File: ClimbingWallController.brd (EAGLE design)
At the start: 100 x 80 mm, 336 parts, among them IC1 74HCT138D, IC2 74HCT138D, IC3 PIC24FJ32GB004, IC4 SN74LV4052AD, IC5 SN74LV4052AD, IC6 TC1015, IC7 NCP1117, J1 PWR, Q1 DPBT8105, Q10 DPBT8105, Q11 DPBT8105, Q12 DPBT8105, Q13 DPBT8105, Q14 DPBT8105, Q15 DPBT8105, Q16 DPBT8105, Q17 NC, Q2 DPBT8105, Q3 DPBT8105, Q4 DPBT8105, Q5 DPBT8105, Q6 DPBT8105, Q7 DPBT8105, Q8 DPBT8105, Q9 DPBT8105, X1 MINI-USB-32005-201

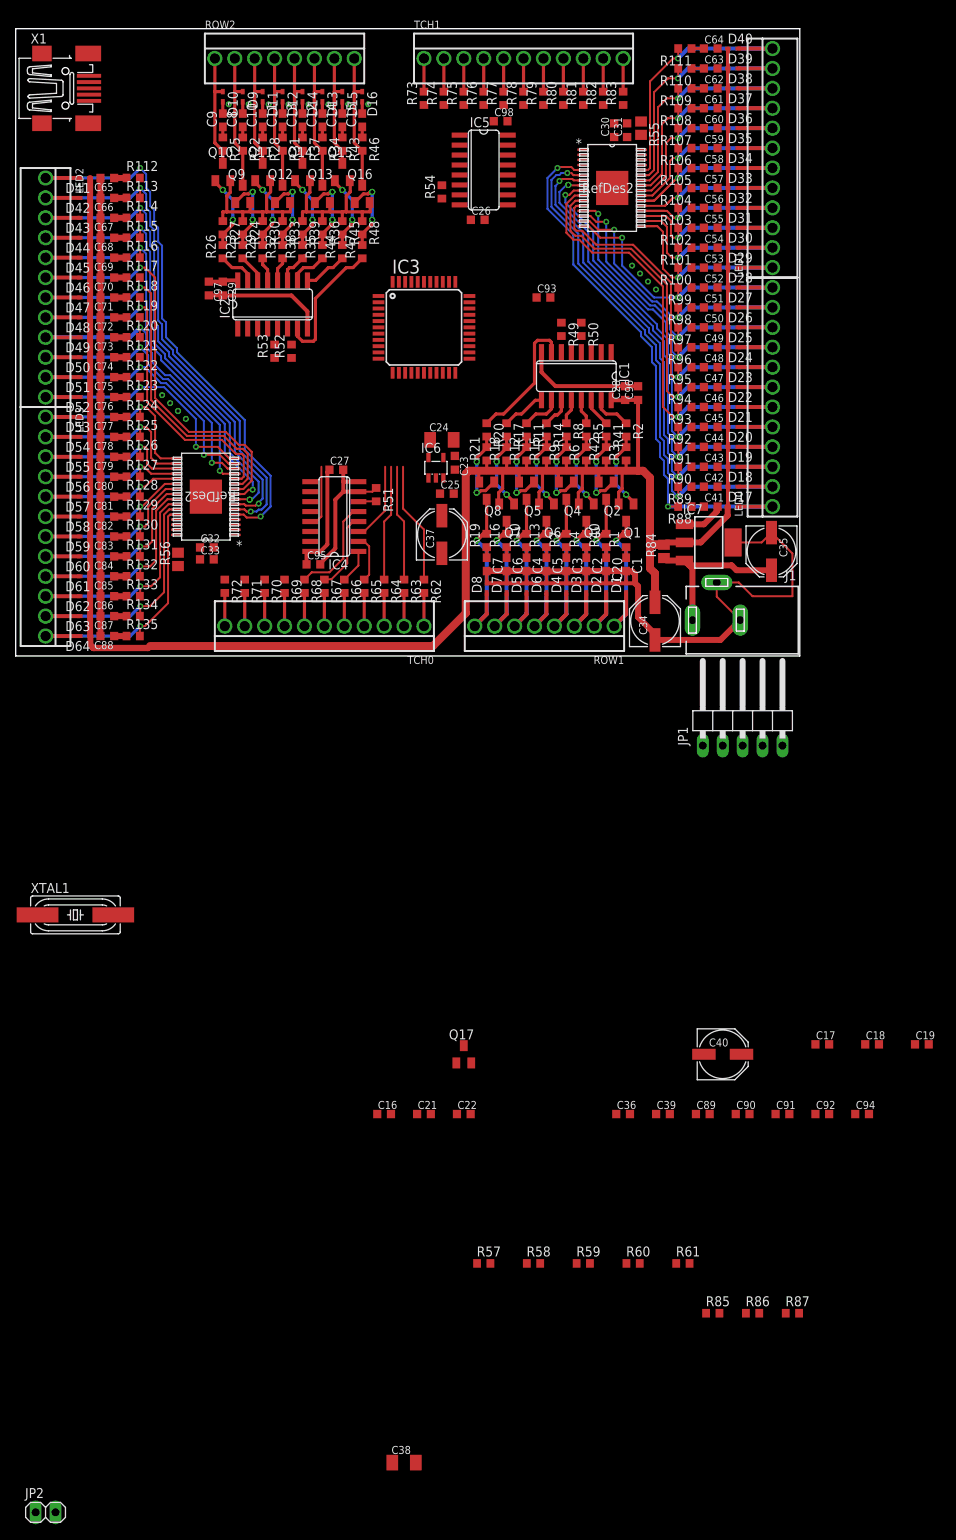
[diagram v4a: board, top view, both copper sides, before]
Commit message: Completed routing of all circuit board elements. Created ground fills, and stitched everything together. Need to review sensitive signal coupling and review decoupling paths. Need to verify footprints.
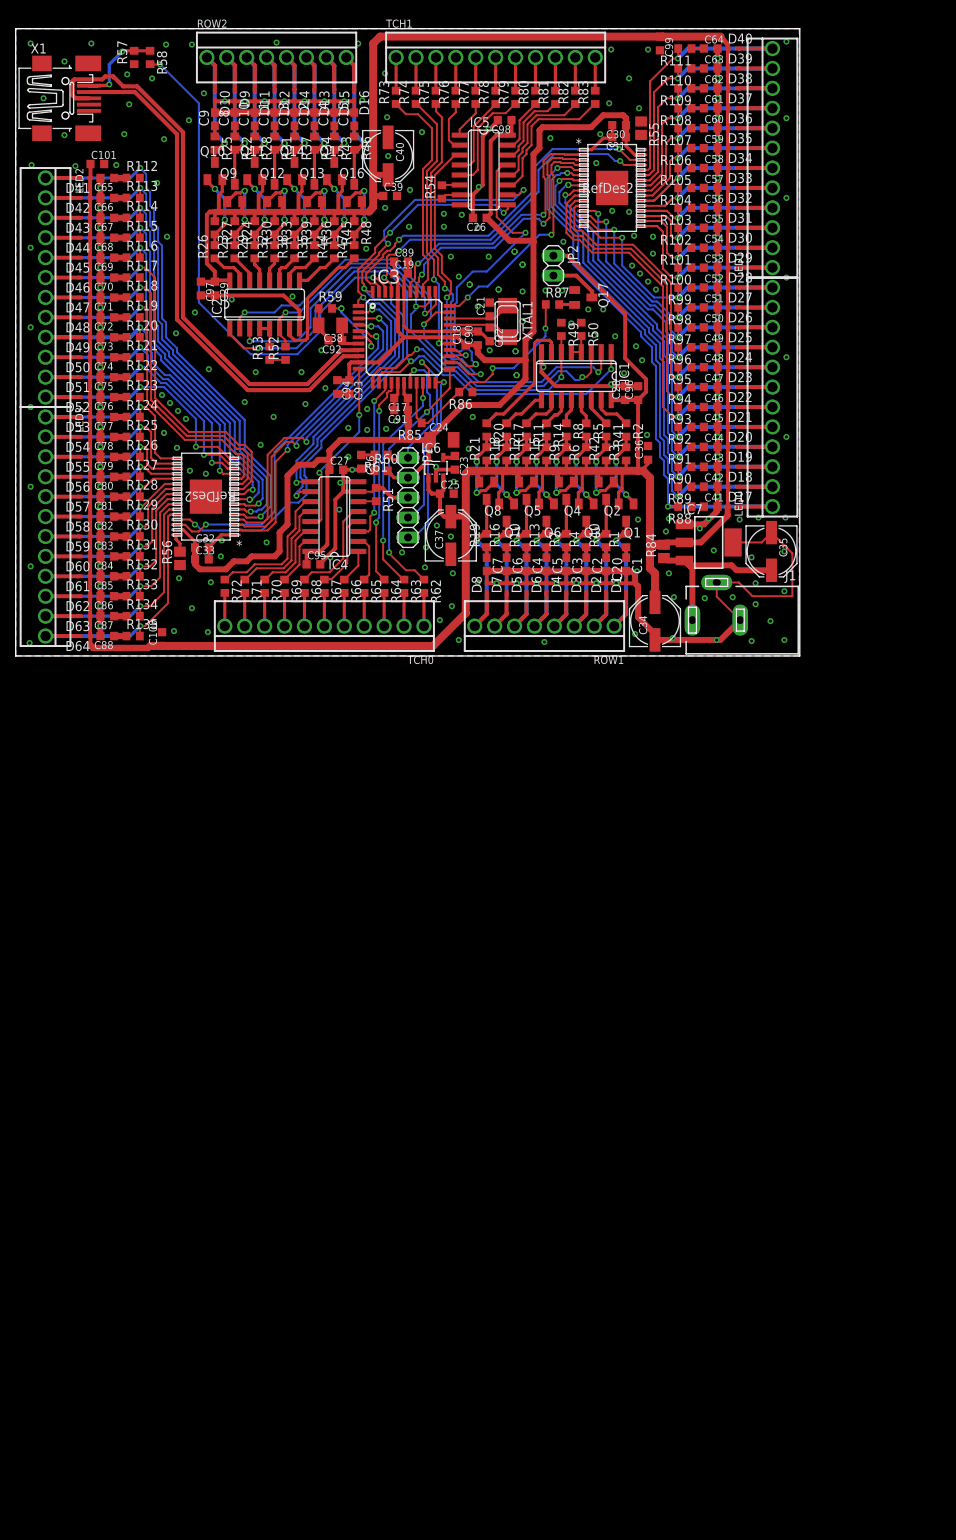
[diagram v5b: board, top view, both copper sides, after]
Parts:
- added C100, C101, C99: 0.1uF, rcl:C0603K
- JP1: device pinhead:1X05/90 -> pinhead:1X05
- XTAL1: device crystal:HC49UP -> Parts:NX5032
- moved JP2 171.7 mm to (68.6, 49.8), turned to 270 degrees
- moved R58 161.4 mm to (17.1, 76.3), turned to 270 degrees
- moved R57 160.1 mm to (15.1, 76.3), turned to 90 degrees
- moved C38 145.3 mm to (40.1, 42.2), turned to 180 degrees
- moved R87 132.2 mm to (68.5, 44.8)
- moved R59 126.2 mm to (39.5, 44.3)
- moved R86 123.0 mm to (57.4, 33.7), turned to 180 degrees
- moved C40 122.2 mm to (47.5, 63.8), turned to 270 degrees
- moved C39 122.2 mm to (47.8, 58.7)
- moved R85 119.7 mm to (50.9, 29.7), turned to 180 degrees
- moved C19 118.6 mm to (49.1, 48.8)
- moved C92 116.6 mm to (40.8, 40.3), turned to 180 degrees
- moved C89 115.3 mm to (49.1, 50.3)
- moved C94 114.3 mm to (41.0, 34.3), turned to 270 degrees
- moved R61 110.1 mm to (46.6, 25.7), turned to 180 degrees
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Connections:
- removed net N$86: R85.1, R86.2
- net +5V: now also C100.1, C101.1, C99.1
- net GND: now also C100.2, C101.2, C99.2
- net OSCI: now also XTAL1.P$1; no longer XTAL1.1
- net OSCO: now also XTAL1.P$2; no longer XTAL1.2
- net TMUX0: now also IC3.14; no longer IC3.11
- net TMUX1: now also IC3.11; no longer IC3.14
- net TOUCH11: now also IC3.36; no longer IC5.1
- net TOUCH12: now also IC3.27; no longer IC5.5
- net TOUCH13: now also IC3.26; no longer IC5.2
- net TOUCH14: now also IC5.2; no longer IC5.4
- net TOUCH15: now also IC5.1; no longer IC5.12
- net TOUCH16: now also IC5.4; no longer IC5.14
- net TOUCH17: now also IC5.5; no longer IC5.15
- net TOUCH18: now also IC5.15; no longer IC5.11
- net TOUCH19: now also IC5.14; no longer IC3.26
- net TOUCH20: now also IC5.12; no longer IC3.27
- net TOUCH21: now also IC5.11; no longer IC3.36
- net VREF+: now also R85.1, R86.2
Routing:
- net +3V3: track 14.5 -> 209.4 mm
- net GND: track 236.1 -> 387.7 mm, vias 0 -> 238
- net +5V: track 338.9 -> 487.4 mm
- net C_BLANK: track 0.00 -> 98.3 mm, vias 0 -> 4
- net RSEL0: track 0.00 -> 76.8 mm, vias 0 -> 3
- net D+: track 0.00 -> 72.7 mm
- net AMSEL0: track 0.00 -> 68.9 mm, vias 0 -> 4
- net RSEL1: track 0.00 -> 68.6 mm, vias 0 -> 3
- net RSEL2: track 0.00 -> 68.5 mm, vias 0 -> 3
- net N$45: track 0.00 -> 66.8 mm, vias 0 -> 2
- net D-: track 0.00 -> 65.8 mm
- net AMSEL1: track 0.00 -> 62.4 mm, vias 0 -> 4
- net C0_SOUT: track 0.00 -> 47.8 mm, vias 0 -> 2
- net C1_SOUT: track 0.00 -> 44.4 mm, vias 0 -> 2
- net C1_LAT: track 0.00 -> 43.4 mm, vias 0 -> 2
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- added copper zone on layer 1, net GND
- added copper zone on layer 16, net GND

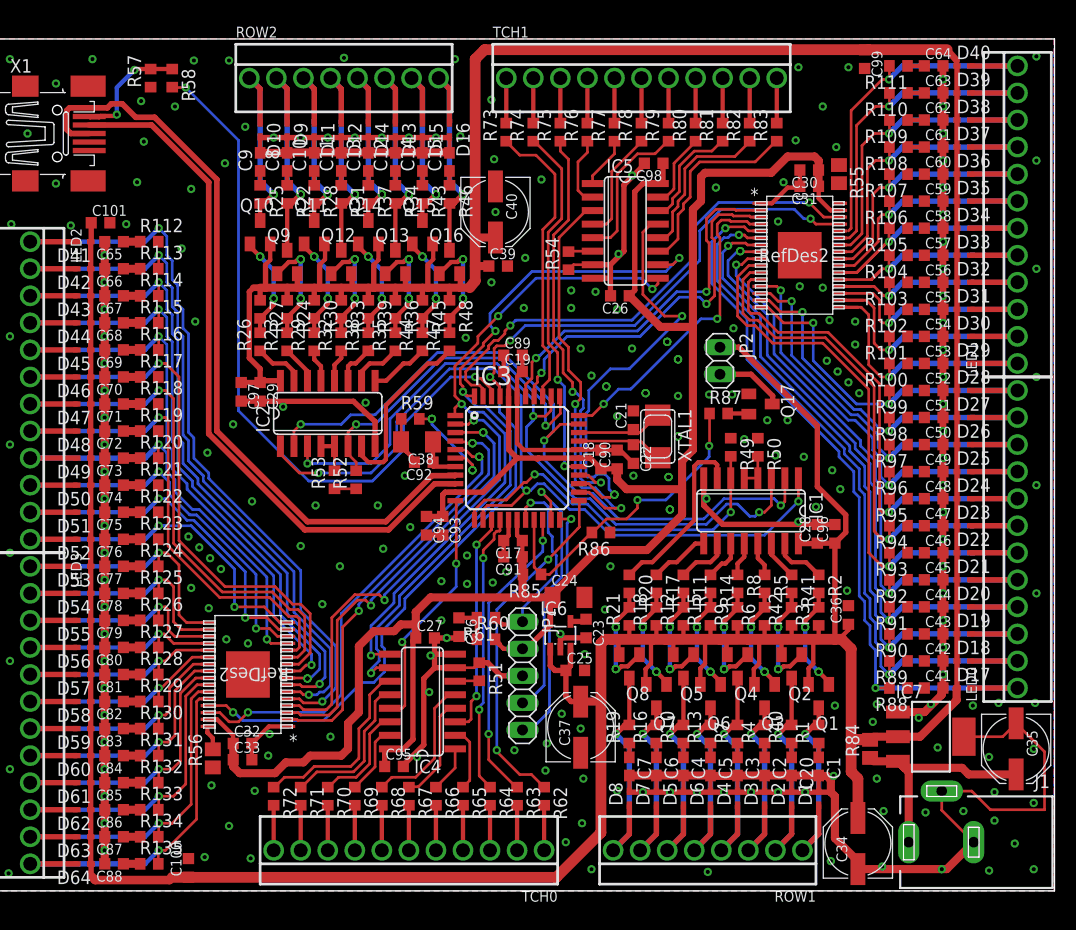
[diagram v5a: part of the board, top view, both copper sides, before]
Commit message: Cleaned up floating ratsnest wires. Cleaned up DRC Errors. Need to check DRC with SEEED's rule set.
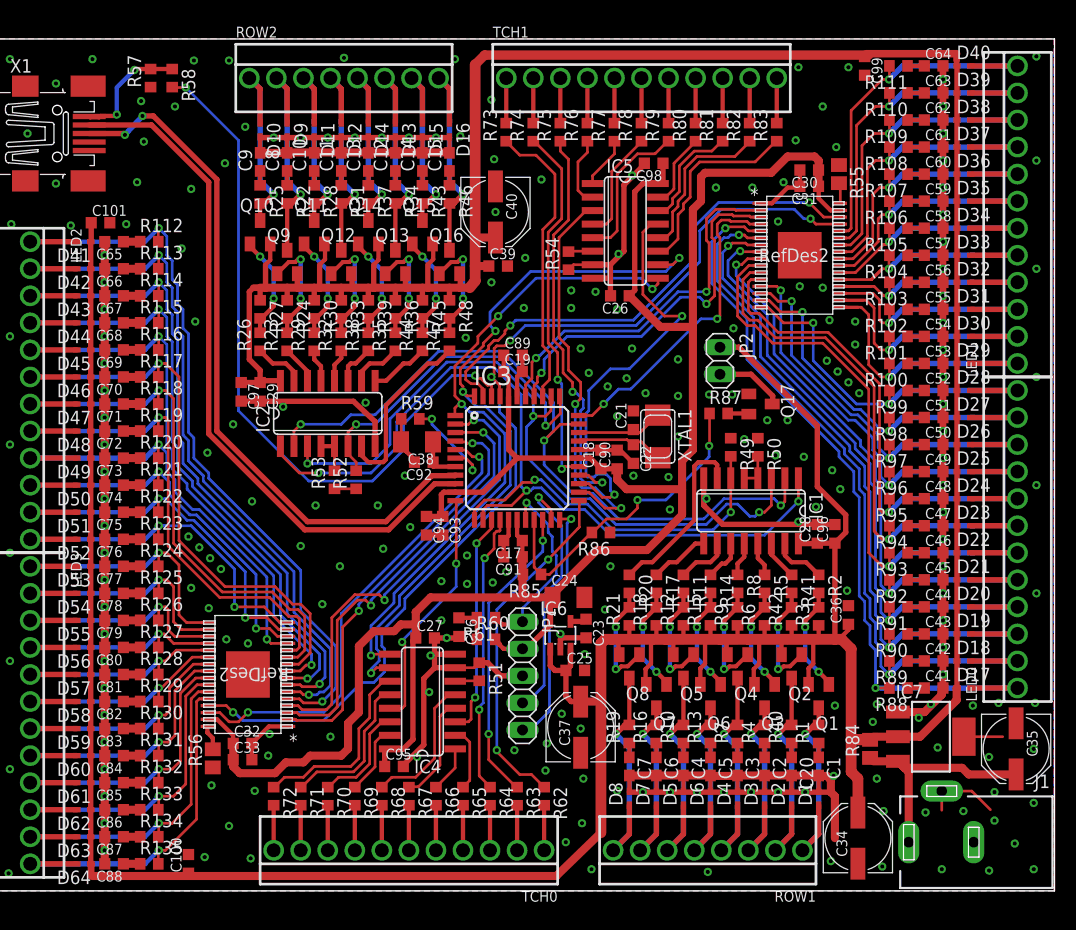
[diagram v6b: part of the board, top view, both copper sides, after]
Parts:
- IC8, IC9: value TLC5952 -> (none)
- R1, R10, R100, R101, R102, R103, R104, R105, R106, R107, R108, R109, R11, R110, R111, R112, R113, R114, R115, R116, R117, R118, R119, R12, R120, R121, R122, R123, R124, R125, R126, R127, R128, R129, R13, R130, R131, R132, R133, R134, R135, R14, R15, R16, R17, R18, R19, R2, R20, R21, R22, R23, R24, R25, R26, R27, R28, R29, R3, R30, R31, R32, R33, R34, R35, R36, R37, R38, R39, R4, R40, R41, R42, R43, R44, R45, R46, R47, R48, R49, R5, R50, R51, R52, R53, R54, R57, R58, R59, R6, R60, R61, R62, R63, R64, R65, R66, R67, R68, R69, R7, R70, R71, R72, R73, R74, R75, R76, R77, R78, R79, R8, R80, R81, R82, R83, R85, R86, R87, R88, R89, R9, R90, R91, R92, R93, R94, R95, R96, R97, R98, R99: device resistor:R0603 -> Parts:R0603
- moved C99 0.64 mm to (82.2, 77.5)
- moved C34 0.51 mm to (81.5, 4.95)
- moved C100 0.38 mm to (18.7, 2.54)
- renumbered U$1 to IC8, U$2 to IC9
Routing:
- net GND: track 387.7 -> 351.9 mm, vias 238 -> 232
- net N$37: track 10.3 -> 0.00 mm
- net D+: track 72.7 -> 66.6 mm, vias 0 -> 2
- net B5: track 29.7 -> 24.1 mm
- net CAIREF: track 0.00 -> 2.02 mm
- net N$99: track 0.00 -> 1.58 mm
- net N$98: track 0.00 -> 1.58 mm
- net N$97: track 0.00 -> 1.58 mm
- net N$96: track 0.00 -> 1.58 mm
- net N$95: track 0.00 -> 1.58 mm
- net N$94: track 0.00 -> 1.58 mm
- net N$93: track 0.00 -> 1.58 mm
- net N$92: track 0.00 -> 1.58 mm
- net N$91: track 0.00 -> 1.58 mm
- net N$90: track 0.00 -> 1.58 mm
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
